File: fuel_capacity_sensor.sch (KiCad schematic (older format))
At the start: 43 parts

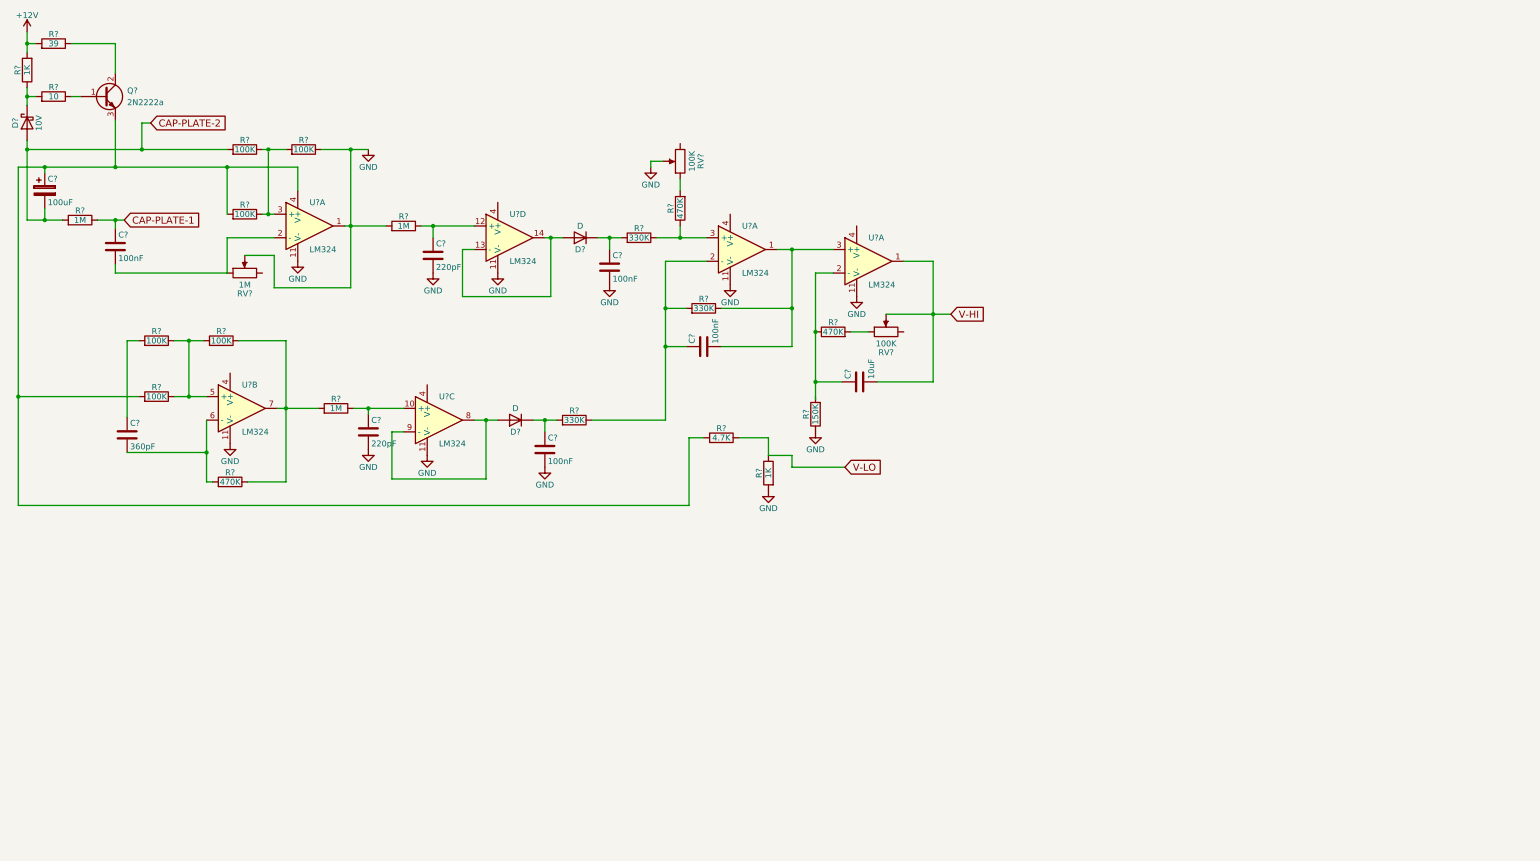
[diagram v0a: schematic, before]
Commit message: Added at90can32 and associated hw
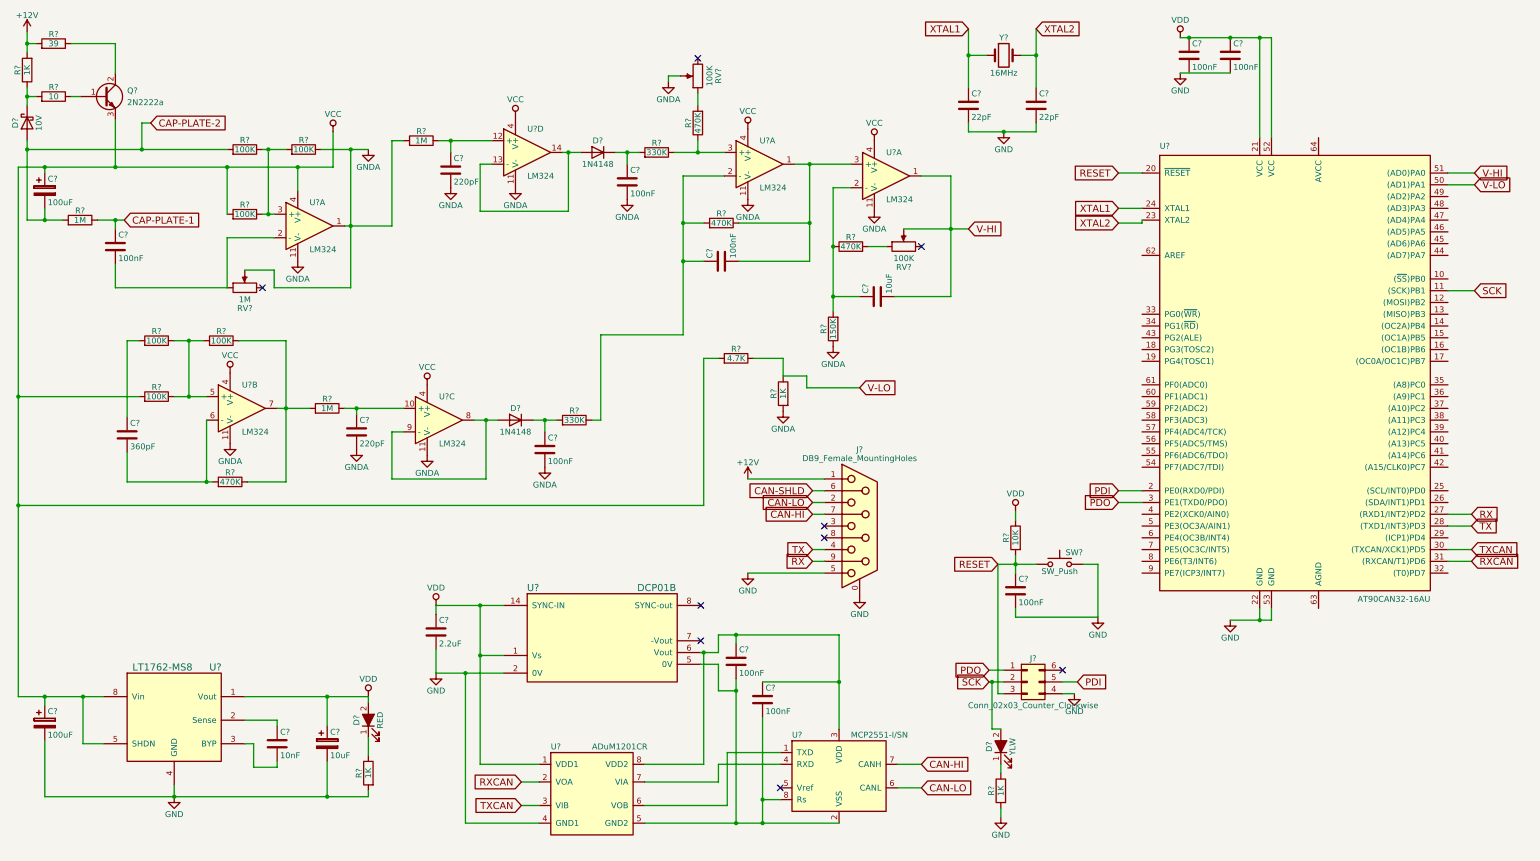
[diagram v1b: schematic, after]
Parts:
- added C? (x5): 100nF, symbol C
- added C? (x2): 22pF, symbol C
- added C?: 2.2uF, symbol C
- added C?: 10nF, symbol C
- added C?: 10uF, symbol CP
- added C?: 100uF, symbol CP
- added D?: RED, symbol LED_ALT
- added D?: YLW, symbol LED_ALT
- added J?: Conn_02x03_Counter_Clockwise, symbol Conn_02x03_Counter_Clockwise
- added J?: DB9_Female_MountingHoles, symbol DB9_Female_MountingHoles
- added R?: 10K, symbol R
- added R? (x2): 1K, symbol R
- added SW?: SW_Push, symbol SW_Push
- added U?: AT90CAN32-16AU, TQFP64, symbol AT90CAN32-16AU
- added U?: LT1762-MS8, symbol LT1762-MS8
- added U?: MCP2551-I/SN, Housings_SOIC:SOIC-8_3.9x4.9mm_Pitch1.27mm, symbol MCP2551-I/SN
- added U?: ADuM1201CR, Housings_SOIC:SOIC-8_3.9x4.9mm_Pitch1.27mm, symbol ADuM1201CR
- added U?: DCP01B, symbol DCP01B
- added Y?: 16MHz, symbol Crystal
- D? (x2): value D -> 1N4148
- R?: value 330K -> 470K
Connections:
- net +12V: now also J?.1
- net GND: now also C?.2, C?.2, C?.2, C?.2, C?.2, C?.2, C?.2, J?.0 (PAD), J?.4 (Pin_4), J?.5, R?.2, R?.2, SW?.2, U?.2 (0V), U?.22 (GND), U?.4 (GND), U?.4 (GND1), U?.53 (GND); no longer C?.2, C?.2, C?.2, C?.2, R?.1, R?.1, R?.2, R?.2, RV?.2, RV?.2, U?.1, U?.11 (V-), U?.11 (V-), U?.11 (V-), U?.11 (V-), U?.11 (V-), U?.11 (V-)
- net V-HI: now also U?.51 ((AD0)PA0)
- net V-LO: now also U?.50 ((AD1)PA1)
- net VCC: now reaches C?.1, Q?.3 (E), R?.2, R?.2, R?.2, U?.4 (V+)
- net VCC: now also U?.4 (V+), U?.4 (V+), U?.4 (V+), U?.4 (V+), U?.4 (V+), C?.1, U?.5 (SHDN), U?.8 (Vin)
- net at C?.1, R?.1, U?.2 (-): now also R?.2
- new net: C?.1, C?.1, U?.3 (VDD), U?.6 (Vout), U?.8 (VDD2)
- new net: C?.2, C?.2, U?.2 (VSS), U?.5 (0V), U?.5 (GND2), U?.8 (Rs)
- new net: C?.1, U?.2 (Sense)
- new net: C?.2, U?.3 (BYP)
- new net: U?.1 (TXD), U?.6 (VOB)
- new net: U?.4 (RXD), U?.7 (VIA)
- new net: D?.1 (K), R?.1 (x2)
- new net CAN-HI: J?.7, U?.7 (CANH)
- new net CAN-LO: J?.2, U?.6 (CANL)
- new net CAN-SHLD: J?.6
- new net GNDA: C?.2, C?.2, C?.2, C?.2, R?.1, R?.1, R?.2, R?.2, RV?.2, RV?.2, U?.1, U?.11 (V-), U?.11 (V-), U?.11 (V-), U?.11 (V-), U?.11 (V-), U?.11 (V-)
- new net PDI: J?.5 (Pin_5), U?.2 (PE0(RXD0/PDI))
- new net PDO: J?.1 (Pin_1), U?.3 (PE1(TXD0/PDO))
- new net RESET: C?.1, J?.3 (Pin_3), R?.2, SW?.1, U?.20 (~RESET)
- new net RX: J?.9, U?.27 ((RXD1/INT2)PD2)
- new net RXCAN: U?.2 (VOA), U?.31 ((RXCAN/T1)PD6)
- new net SCK: D?.2 (A), J?.2 (Pin_2), U?.11 ((SCK)PB1)
- new net TX: J?.4, U?.28 ((TXD1/INT3)PD3)
- new net TXCAN: U?.3 (VIB), U?.30 ((TXCAN/XCK1)PD5)
- new net VDD: C?.1, C?.1, C?.1, C?.1, D?.2 (A), R?.1, U?.1 (VDD1), U?.1 (Vout), U?.1 (Vs), U?.14 (SYNC-IN), U?.21 (VCC), U?.52 (VCC)
- new net XTAL1: C?.1, U?.24 (XTAL1), Y?.1
- new net XTAL2: C?.1, U?.23 (XTAL2), Y?.2
- no-connect marks 0 -> 9
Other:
- moved on the sheet: C?, D?, R?, RV?, U?A, U?D

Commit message: Added at90can32 and footprints
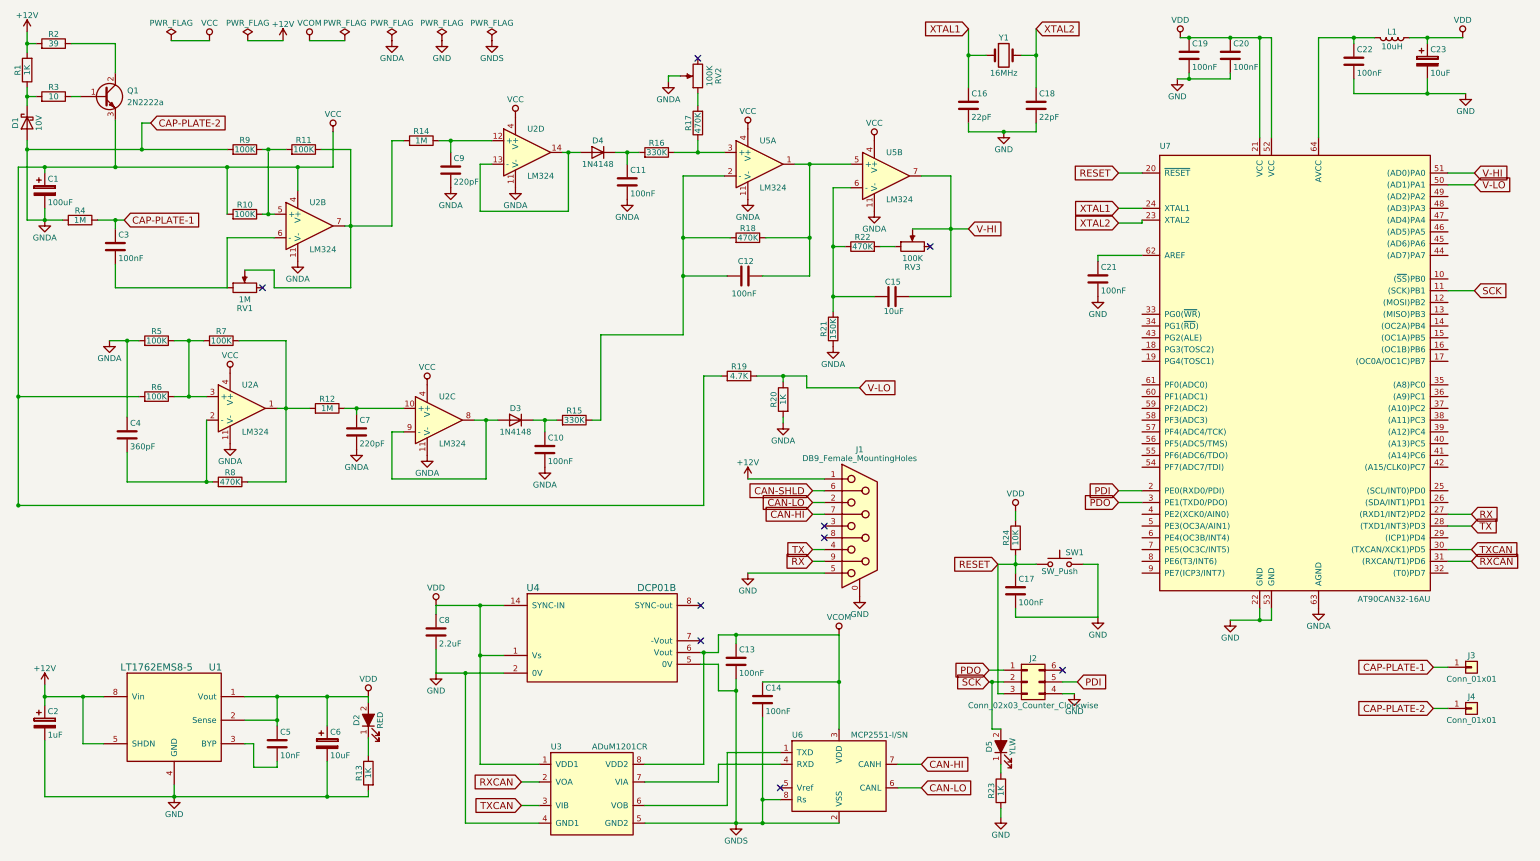
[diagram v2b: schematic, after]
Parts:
- removed U?: DCP01B, symbol DCP01B
- added C21, C22: 100nF, Capacitors_SMD:C_0603, symbol C
- added C23: 10uF, Capacitors_Tantalum_SMD:CP_Tantalum_Case-A_EIA-3216-18_Reflow, symbol CP
- added J3, J4: Conn_01x01, CustomComponents:FASTON-187-vert-90deg-terminal, symbol Conn_01x01
- added L1: 10uH, Inductors_SMD:L_1206, symbol L
- added U4: DCP01B, CustomComponents:DCP01B_SO_7_14, symbol DCP01B
- C1, C10, C11, C12, C13, C14, C15, C16, C17, C18, C19, C20, C3, C4, C5, C6, C7, C8, C9: renamed from C?; footprint (none) -> Capacitors_SMD:C_0603
- C2: renamed from C?; value 100uF -> 1uF; footprint (none) -> Capacitors_SMD:C_0603
- D1, D2, D3, D4, D5: renamed from D?; footprint (none) -> Diodes_SMD:D_SOD-123F
- J2: renamed from J?; footprint (none) -> Pin_Headers:Pin_Header_Straight_2x03_Pitch2.54mm
- Q1: renamed from Q?; footprint (none) -> TO_SOT_Packages_THT:TO-92_Inline_Narrow_Oval
- R1, R10, R11, R12, R13, R14, R15, R16, R17, R18, R19, R2, R20, R21, R22, R23, R24, R3, R4, R5, R6, R7, R8, R9: renamed from R?; footprint (none) -> Resistors_SMD:R_0603
- RV1, RV2, RV3: renamed from RV?; footprint (none) -> Potentiometers:Potentiometer_Trimmer_Copal_CT-6EP
- SW1: renamed from SW?; footprint (none) -> CustomComponents:switch-kpt-1187B-SMD
- U1: renamed from U?; value LT1762-MS8 -> LT1762EMS8-5; footprint (none) -> Housings_SSOP:MSOP-8_3x3mm_Pitch0.65mm
- U2, U5: renamed from U?; footprint (none) -> Housings_SOIC:SOIC-16W_5.3x10.2mm_Pitch1.27mm
- U7: renamed from U?; footprint TQFP64 -> Housings_QFP:TQFP-64_10x10mm_Pitch0.5mm
- Y1: renamed from Y?; footprint (none) -> Crystals:Crystal_SMD_HC49-SD
- gave numbers to parts that had none: 3
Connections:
- net CAP-PLATE-2 is gone; now on net GNDA: C1.2, D1.2 (A), R4.2, R9.2
- net +12V: now also C2.1, U1.5 (SHDN), U1.8 (Vin)
- net CAP-PLATE-1: now also J3.1 (Pin_1)
- net GND: now also C19.2, C21.2, C22.2, C23.2, U4.2 (0V)
- net GNDA: now also C4.1, R5.2, U7.63 (AGND), J4.1 (Pin_1); no longer R11.1, R14.2, RV1.2, U2.1
- net V-HI: now also U5.7; no longer U5.1
- net VCC: no longer C2.1, U1.5 (SHDN), U1.8 (Vin)
- net VDD: now also C5.1, U1.2 (Sense), C23.1, L1.1, U4.1 (Vs), U4.14 (SYNC-IN)
- net at C3.2, RV1.1: now also U2.6 (-); no longer U2.2 (-)
- net at R10.1: now also U2.5 (+); no longer U2.3 (+)
- net at R5.1, R6.1, R7.2: now also U2.3 (+); no longer U2.5 (+)
- net at C4.2, R8.2: now also U2.2 (-); no longer U2.6 (-)
- net at R12.2, R7.1, R8.1: now also U2.1; no longer U2.7
- net at C12.2, R18.1, U5.1: now also U5.5 (+); no longer U5.3 (+)
- net at C15.1, R21.2, R22.1: now also U5.6 (-); no longer U5.2 (-)
- net at U7.62 (AREF): now also C21.1
- net at U7.64 (AVCC): now also C22.1, L1.2
- net VCOM: now reaches C13.1, C14.1, U3.8 (VDD2), U6.3 (VDD)
- net VCOM: now also U4.6 (Vout)
- net GNDS: now reaches C13.2, C14.2, U3.5 (GND2), U6.2 (VSS), U6.8 (Rs)
- net GNDS: now also U4.5 (0V)
- new net: R11.1, R14.2, RV1.2, U2.7
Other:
- moved on the sheet: C12, C15, R18, R19, R20, R22, RV3

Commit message: Updated schematic and footprints
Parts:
- removed D1: 10V, Diodes_SMD:D_SOD-123F, symbol D_Schottky
- removed J1: DB9_Female_MountingHoles, symbol DB9_Female_MountingHoles
- removed J3, J4: Conn_01x01, CustomComponents:FASTON-187-vert-90deg-terminal, symbol Conn_01x01
- added D1: 10V, Diodes_SMD:D_SOD-123F, symbol D_Zener
- added D6: YLW, Diodes_SMD:D_SOD-123F, symbol LED_ALT
- added J1, J2: Conn_01x06_Male, Connectors_JST:JST_XH_B06B-XH-A_06x2.50mm_Straight, symbol Conn_01x06_Male
- added J4: Conn_Coaxial, Connectors:bnc-ci, symbol Conn_Coaxial
- added J5: Conn_01x06_Male, Pin_Headers:Pin_Header_Straight_1x06_Pitch2.54mm, symbol Conn_01x06_Male
- added R25: 1K, Resistors_SMD:R_0603, symbol R
- added TP1, TP2, TP3, TP4: TEST, Measurement_Points:Test_Point_Keystone_5015_Micro-Minature, symbol TEST
- renumbered J2 to J3
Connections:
- net +12V: now also J1.2 (Pin_2), J2.2 (Pin_2)
- net CAN-HI: now also J1.4 (Pin_4), J2.4 (Pin_4)
- net CAN-LO: now also J1.5 (Pin_5), J2.5 (Pin_5)
- net CAN-SHLD: now also J1.1 (Pin_1), J2.1 (Pin_1)
- net CAP-PLATE-1: now also J4.2 (Ext)
- net GND: now also J1.6 (Pin_6), J2.6 (Pin_6), J5.1 (Pin_1), J5.2 (Pin_2), R25.2
- net GNDA: now also D1.2 (A), J4.1 (In)
- net GNDS: no longer C13.2, C14.2, U3.5 (GND2), U4.5 (0V), U6.2 (VSS), U6.8 (Rs)
- net RX: now also J5.4 (Pin_4)
- net TX: now also J5.5 (Pin_5)
- net VCC: now also TP1.1
- net at R11.1, R14.2, RV1.2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: now also TP2.1, TP4.1
- net at R12.2, R7.1, R8.1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: now also TP3.1
- net at R1.1, R3.2: now also D1.1 (K)
- net at U7.35 ((A8)PC0): now also D6.2 (A)
- new net: D6.1 (K), R25.1
- new net CAN-GND: C13.2, C14.2, J1.3 (Pin_3), J2.3 (Pin_3), U3.5 (GND2), U4.5 (0V), U6.2 (VSS), U6.8 (Rs)
- no-connect marks 9 -> 52
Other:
- moved on the sheet: R19, R20

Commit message: Many updates
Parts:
- removed C2: 1uF, Capacitors_SMD:C_0603, symbol CP
- removed C6: 10uF, Capacitors_SMD:C_0603, symbol CP
- removed Q1: 2N2222a, TO_SOT_Packages_THT:TO-92_Inline_Narrow_Oval, symbol Q_NPN_BCE
- removed U1: LT1762EMS8-5, Housings_SSOP:MSOP-8_3x3mm_Pitch0.65mm, symbol LT1762-MS8
- removed U5: LM324, Housings_SOIC:SOIC-16W_5.3x10.2mm_Pitch1.27mm, symbol LM324
- added C2: .33uF, Capacitors_SMD:C_0603, symbol C
- added C24, C6: 100nF, Capacitors_SMD:C_0603, symbol C
- added C25, C26: 10nF, Capacitors_SMD:C_0603, symbol C
- added F1: Fuse, Fuse_Holders_and_Fuses:Fuse_SMD1206_Reflow, symbol Fuse
- added Q1: BCW65CLT1G, TO_SOT_Packages_SMD:SOT-23, symbol 2N3055
- added TP5, TP6: TEST, Measurement_Points:Test_Point_Keystone_5015_Micro-Minature, symbol TEST
- added U1: LM78M05_TO252, TO_SOT_Packages_SMD:TO-252-2, symbol LM78M05_TO252
- added U5: LT1490A, Housings_SOIC:SOIC-8_3.9x4.9mm_Pitch1.27mm, symbol LT1492
- C5: value 10nF -> 100nF
- J1: value Conn_01x06_Male -> CAN1
- J2: value Conn_01x06_Male -> CAN2
- J3: value Conn_02x03_Counter_Clockwise -> ISP
- J5: value Conn_01x06_Male -> SERIAL
- U2: value LM324 -> LT1491A; footprint Housings_SOIC:SOIC-16W_5.3x10.2mm_Pitch1.27mm -> Housings_SOIC:SOIC-16_3.9x9.9mm_Pitch1.27mm
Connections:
- net +12V: now also C2.1, F1.1, U1.1 (VI); no longer J1.2 (Pin_2), J2.2 (Pin_2)
- net CAN-GND: now also C24.1
- net GND: now also C5.1, C2.2, C6.2, U1.2 (GND)
- net GNDA: now also TP2.1, C25.2, C26.2, U5.4 (V-), U5.4 (V-)
- net V-HI: now also U5.7
- net VCC: now also C25.1, C26.1, Q1.2 (E), U5.8 (V+), U5.8 (V+)
- net VCOM: now also C24.2
- net VDD: now also C5.2, C6.1, U1.3 (VO); no longer C5.1
- net at R11.1, R14.2, RV1.2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: no longer TP2.1
- net at R2.1: now also Q1.3 (C)
- net at R3.1: now also Q1.1 (B)
- net at C11.1, D4.1 (K), R16.2: now also TP6.1
- net at C10.1, D3.1 (K), R15.2: now also TP5.1
- net at C12.2, R18.1: now also U5.1, U5.5 (+)
- net at C12.1, R15.1, R18.2: now also U5.2 (-)
- net at R16.1, R17.1: now also U5.3 (+)
- net at C15.1, R21.2, R22.1: now also U5.6 (-)
- new net: F1.2, J1.2 (Pin_2), J2.2 (Pin_2)
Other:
- note added: "Op-Amp Bypass"
- moved on the sheet: C1, C3, D2, R13, R4, TP2

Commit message: Fixed ISP header
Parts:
- removed J3: ISP, Pin_Headers:Pin_Header_Straight_2x03_Pitch2.54mm, symbol Conn_02x03_Counter_Clockwise
- added J3: ISP, symbol Conn_02x03_Odd_Even
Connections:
- net GND: now also J3.6 (Pin_6)
- net PDI: now also J3.4 (Pin_4)
- net PDO: now also J3.1 (Pin_1)
- net RESET: now also J3.5 (Pin_5)
- net SCK: now also J3.3 (Pin_3)
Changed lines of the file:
@@
 Text GLabel 8650 725  0    60   Input ~ 0
 XTAL1
-$Comp
-L Conn_02x03_Counter_Clockwise J3
-U 1 1 5B6FFEB7
-P 9150 6275
-F 0 "J3" H 9200 6475 50  0000 C CNN
-F 1 "ISP" H 9200 6075 50  0000 C CNN
-F 2 "Pin_Headers:Pin_Header_Straight_2x03_Pitch2.54mm" H 9150 6275 50  0001 C CNN
-F 3 "" H 9150 6275 50  0001 C CNN
-	1    9150 6275
-	1    0    0    -1
-$EndComp
 Text GLabel 9575 6275 2    60   Input ~ 0
 PDI
@@
 Text Notes 4450 3150 0    60   ~ 0
 Op-Amp Bypass
+$Comp
+L Conn_02x03_Odd_Even J3
+U 1 1 5BB6F199
+P 9150 6275
+F 0 "J3" H 9200 6475 50  0000 C CNN
+F 1 "ISP" H 9200 6075 50  0000 C CNN
+F 2 "" H 9150 6275 50  0001 C CNN
+F 3 "" H 9150 6275 50  0001 C CNN
+	1    9150 6275
+	1    0    0    -1
+$EndComp
 $EndSCHEMATC

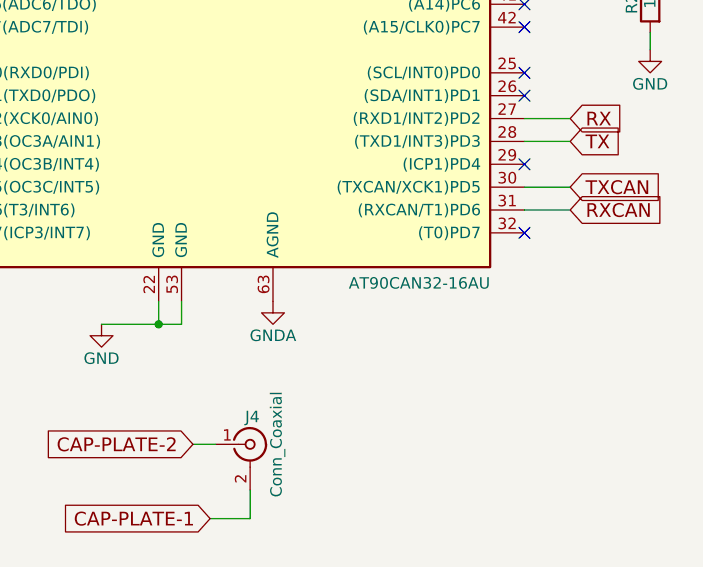
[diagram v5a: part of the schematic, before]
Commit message: New version of kicad changes
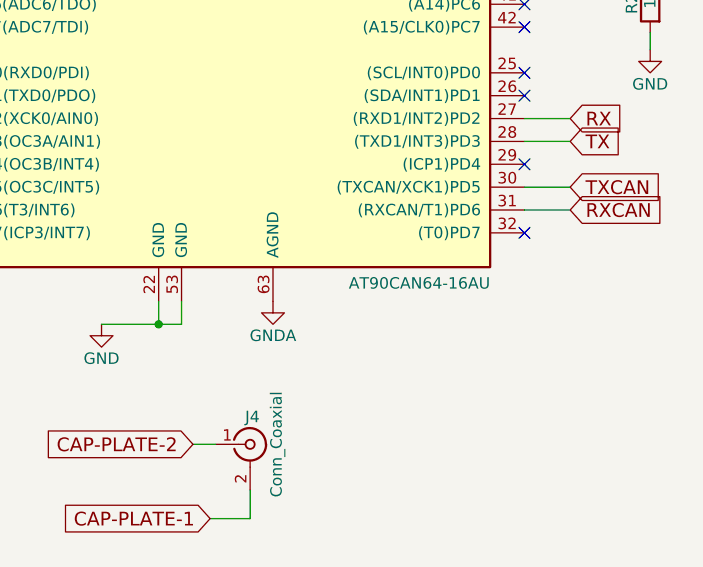
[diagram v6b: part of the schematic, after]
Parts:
- removed U7: AT90CAN32-16AU, Housings_QFP:TQFP-64_10x10mm_Pitch0.5mm, symbol AT90CAN32-16AU
- added U7: AT90CAN64-16AU, Housings_QFP:TQFP-64_10x10mm_Pitch0.5mm, symbol AT90CAN64-16AU
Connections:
- net GND: now also U7.22 (GND), U7.53 (GND)
- net GNDA: now also U7.63 (AGND)
- net PDI: now also U7.2 (PE0(RXD0/PDI))
- net PDO: now also U7.3 (PE1(TXD0/PDO))
- net RESET: now also U7.20 (~RESET)
- net RX: now also U7.27 ((RXD1/INT2)PD2)
- net RXCAN: now also U7.31 ((RXCAN/T1)PD6)
- net SCK: now also U7.11 ((SCK)PB1)
- net TX: now also U7.28 ((TXD1/INT3)PD3)
- net TXCAN: now also U7.30 ((TXCAN/XCK1)PD5)
- net V-HI: now also U7.51 ((AD0)PA0)
- net V-LO: now also U7.50 ((AD1)PA1)
- net VDD: now also U7.21 (VCC), U7.52 (VCC)
- net XTAL1: now also U7.24 (XTAL1)
- net XTAL2: now also U7.23 (XTAL2)
- net at D6.2 (A): now also U7.35 ((A8)PC0)
- net at C21.1: now also U7.62 (AREF)
- net at C22.1, L1.2: now also U7.64 (AVCC)
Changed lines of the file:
@@
-$EndComp
-$Comp
-L AT90CAN32-16AU U7
-U 1 1 5B6F4BF4
-P 11425 3650
-F 0 "U7" H 10275 5550 50  0000 L BNN
-F 1 "AT90CAN32-16AU" H 12575 1700 50  0000 R BNN
-F 2 "Housings_QFP:TQFP-64_10x10mm_Pitch0.5mm" H 11475 3650 50  0001 C CNN
-F 3 "" H 11425 3650 50  0001 C CNN
-	1    11425 3650
-	1    0    0    -1
 $EndComp
 $Comp
@@
 	1    0    0    -1
 $EndComp
+$Comp
+L AT90CAN64-16AU U7
+U 1 1 5BBA7199
+P 11425 3650
+F 0 "U7" H 10275 5550 50  0000 L BNN
+F 1 "AT90CAN64-16AU" H 12575 1700 50  0000 R BNN
+F 2 "Housings_QFP:TQFP-64_10x10mm_Pitch0.5mm" H 11475 3650 50  0001 C CNN
+F 3 "" H 11425 3650 50  0001 C CNN
+	1    11425 3650
+	1    0    0    -1
+$EndComp
